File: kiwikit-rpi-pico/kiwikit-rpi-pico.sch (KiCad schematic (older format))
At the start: 50 parts, among them J1 Conn_02x04_Odd_Even, J2 Conn_01x03, J3 Conn_01x06, J4 Conn_01x08, J5 Conn_01x09, J6 Conn_01x03, J7 Conn_01x03, SW0 SW_Push, SW1 SW_Push, SW2 SW_Push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

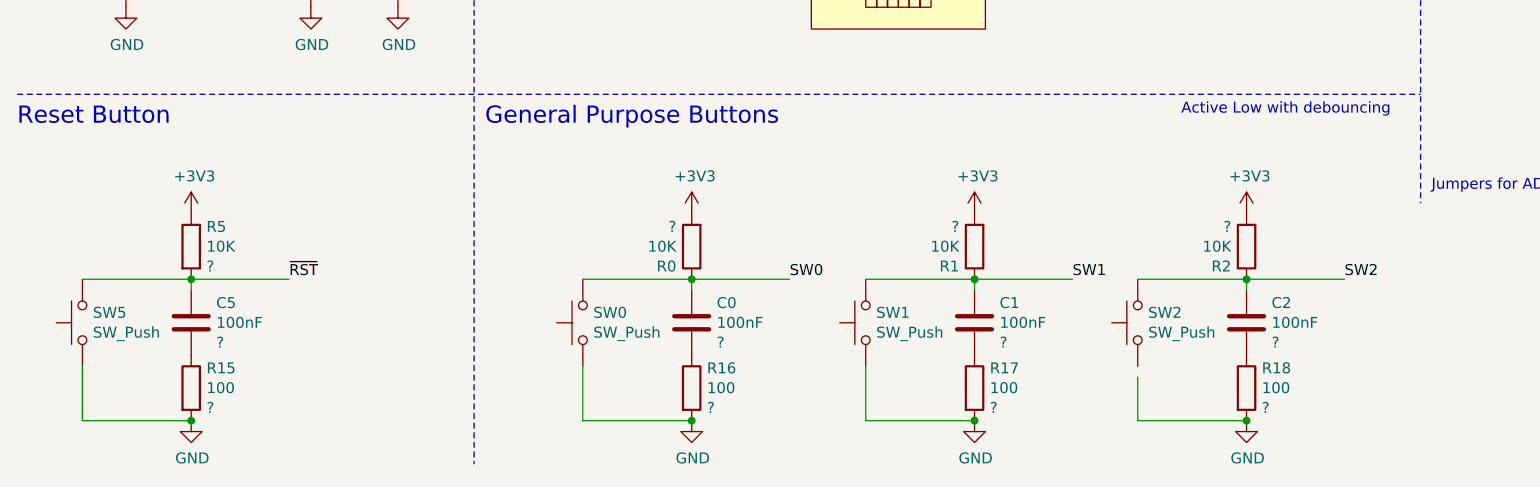
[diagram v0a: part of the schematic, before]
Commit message: Update to version 0.3, adjust debouncer layout.
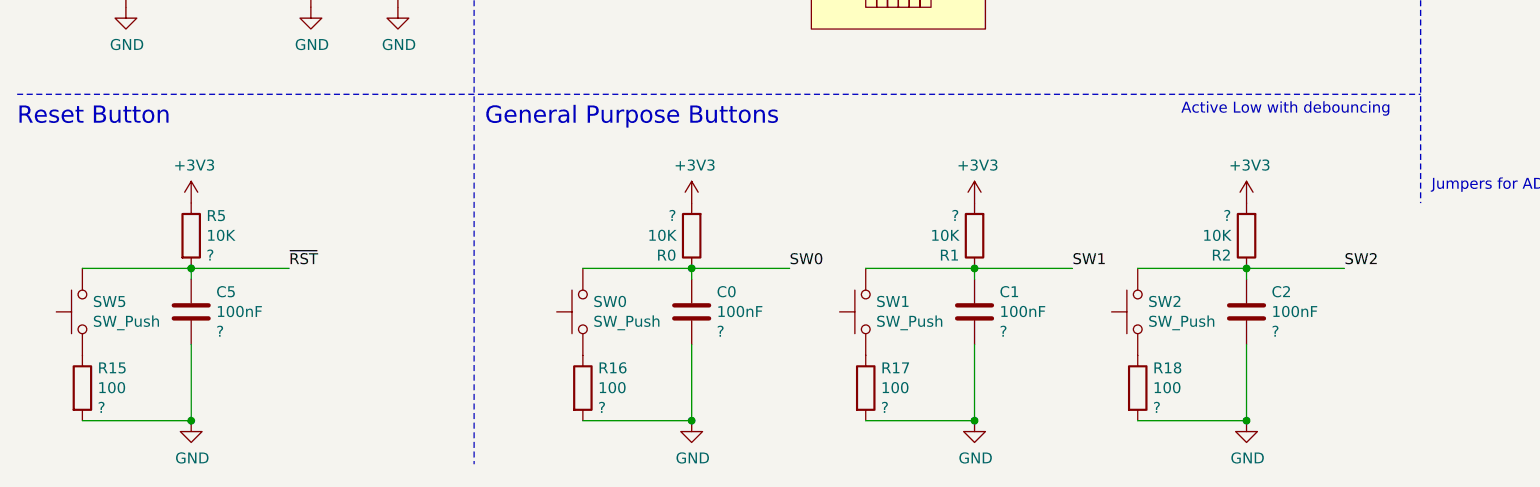
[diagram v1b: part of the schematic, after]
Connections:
- net GND: now also C0.1, C1.1, C2.1, C5.1; no longer SW0.1, SW1.1, SW5.1
- net at R17.1: now also SW1.1; no longer C1.1
- net at R18.1: now also SW2.1; no longer C2.1
- net at R16.1: now also SW0.1; no longer C0.1
- net at R15.1: now also SW5.1; no longer C5.1
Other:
- moved on the sheet: C0, C1, C2, C5, R0, R1, R15, R16, R17, R18, R2, R5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
